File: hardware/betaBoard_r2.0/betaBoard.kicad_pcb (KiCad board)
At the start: 2 copper layers, 70 x 45 mm, 141 parts, among them J1 DNP, J2 AMPHENOL_10103592-0001LF, J3 DNP, J4 DNP, J5 DNP, J6 DNP, SW1 TS-1187A-B-A-B, SW2 TS-1187A-B-A-B, U1 AMS1117-3.3_SOT223, U2 W25Q128JVSIQ, U3 RP2040, U4 LM358, U5 LM358, U6 LM358, U7 LM358, Y1 X322512MSB4SI

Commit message: main r2.0 design done
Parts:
- removed C35, C41: 47p, Capacitor_SMD:C_0603_1608Metric
- removed C36: 100n, Capacitor_SMD:C_0603_1608Metric
- removed C37, C38: 10p, Capacitor_SMD:C_0603_1608Metric
- removed C39: 470n, Capacitor_SMD:C_0603_1608Metric
- removed C40: 1u, Capacitor_SMD:C_0603_1608Metric
- removed C42: 10u, Capacitor_SMD:C_1206_3216Metric
- removed C44, C46, C47: 10u, Capacitor_SMD:C_0603_1608Metric
- removed D16: DNP, OptoDevice:Osram_BPW34S-SMD
- removed D17, D18, D24, D25: 1N5819WS, Diode_SMD:D_SOD-323
- removed D20, D22, D23: ZMM3V3-M, Diode_SMD:D_MiniMELF
- removed J1: DNP, betaBoard:PinHeader_1x02_P2.54mm_castellation
- removed J3: DNP, Connector_PinSocket_2.54mm:PinSocket_1x02_P2.54mm_Vertical
- removed JP1: DNP, Jumper:SolderJumper-2_P1.3mm_Bridged2Bar_Pad1.0x1.5mm
- removed U7: LM358, Package_SO:SOIC-8_3.9x4.9mm_P1.27mm
- added H7: M3 Hole, MountingHole:MountingHole_2.7mm_M2.5_DIN965_Pad, F.Cu at (90.0, 53.0)
- added H8: M3 Hole, MountingHole:MountingHole_2.7mm_M2.5_DIN965_Pad, F.Cu at (53.0, 97.0)
- added H9: M3 Hole, MountingHole:MountingHole_2.7mm_M2.5_DIN965_Pad, F.Cu at (53.0, 53.0)
- C1: value 10u -> 100u
- C19, C31: value 10p -> 100n
- C20, C32: value 10p -> 1u
- C21, C33: value 470n -> 10p
- C22: value 1u -> 100u; footprint Capacitor_SMD:C_0603_1608Metric -> Capacitor_SMD:C_1206_3216Metric
- C23: value 47p -> 100n
- C25: value 10p -> 10u
- C26: value 10p -> 2p2
- C27: value 470n -> 100n
- C29: value 47p -> 10p
- C30: value 100n -> 10p
- C34: value 1u -> 10p
- D1, D13, D5, D9: moved to F.Cu
- D10, D11, D14, D6, D7: value BPW34-SMD -> ZMM3V3-M; footprint betaBoard:Osram_BPW34S-SMD_hole -> Diode_SMD:D_MiniMELF
- D12, D4, D8: value DNP -> ZMM3V3-M; footprint OptoDevice:Osram_BPW34S-SMD -> Diode_SMD:D_MiniMELF; moved to F.Cu
- D15, D2, D3: value BPW34-SMD -> DNP; footprint betaBoard:Osram_BPW34S-SMD_hole -> OptoDevice:Osram_BPW34S-SMD
- R13, R21: value 47k -> 1k
- R14, R22, R30: value 150k -> 10k
- R15, R31: value 47M -> 10k
- R16, R24: value 4K7 -> 1k
- R17: value 10k -> 1k
- R19, R27: value 1M -> 100k
- R2, R3, R4, R5: value 1k -> 10k
- R23: value 47M -> 22M
- R26, R41, R42, R44: value 10k -> 100k
- R29: value 47k -> 10k
- R32, R40: value 4K7 -> 10k
- R33: value 10k -> 4R7
- R34, R36: value 10k -> 0
- R35: value 1M -> 1k
- R37: value 47k -> 10M
- R38: value 150k -> 1k
- R39: value 47M -> 1k
- R43: value 1M -> 10k
- R45: value 0 -> DNP
- U4, U5, U6: value LM358 -> MCP6232
- moved H6 75.7 mm to (116.0, 92.5)
- moved H5 70.7 mm to (57.5, 97.0)
- moved R31 40.2 mm to (61.8, 75.5), turned to -90 degrees
- moved H4 37.3 mm to (56.5, 56.0)
- moved R32 33.1 mm to (63.4, 75.5)
- moved C34 32.5 mm to (110.9, 89.0), turned to 180 degrees
- moved R30 31.8 mm to (76.2, 81.8), turned to -90 degrees
- moved R29 31.8 mm to (77.7, 81.8)
- moved R36 29.8 mm to (110.9, 85.8), turned to 0 degrees
- moved D12 28.1 mm to (95.3, 88.7)
- moved C25 27.2 mm to (110.9, 84.2), turned to 0 degrees
- moved R44 26.6 mm to (110.9, 90.7), turned to 0 degrees
- moved D14 26.3 mm to (93.0, 88.7), turned to 90 degrees
- moved C22 25.8 mm to (96.1, 58.7), turned to 180 degrees
- moved D5 25.7 mm to (116.8, 61.3), turned to 90 degrees
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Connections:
- C1 pad 1: /LDO_IN -> /5V_USB
- C19 pad 1: /particle_sensor_array/Diodes -> Net-(U4B-+)
- C20 pad 1: Net-(C19-Pad2) -> Net-(U4A-+)
- C20 pad 2: Net-(C20-Pad2) -> GND
- C21 pad 1: Net-(C20-Pad2) -> Net-(U4A--)
- C22 pad 1: Net-(U4B-+) -> VCC
- C23 pad 1: Net-(U4B--) -> VCC
- C23 pad 2: Net-(C23-Pad2) -> GND
- C25 pad 1: /particle_sensor_array1/Diodes -> Net-(D11-K)
- C25 pad 2: Net-(C25-Pad2) -> GND
- C26 pad 1: Net-(C25-Pad2) -> Net-(U5A--)
- C26 pad 2: Net-(C26-Pad2) -> Net-(U4B-+)
- C27 pad 1: Net-(C26-Pad2) -> Net-(U4B-+)
- C30 pad 1: VCC -> Net-(U6A--)
- C30 pad 2: GND -> Net-(C30-Pad2)
- C31 pad 1: /particle_sensor_array2/Diodes -> Net-(C31-Pad1)
- C32 pad 1: Net-(C31-Pad2) -> Net-(U6B-+)
- C32 pad 2: Net-(C32-Pad2) -> GND
- C33 pad 1: Net-(C32-Pad2) -> Net-(U6B--)
- C34 pad 1: Net-(U6B-+) -> Net-(C30-Pad2)
- C34 pad 2: GND -> Net-(C31-Pad1)
- C45 pad 1: Net-(U5A-+) -> Net-(D4-K)
- D10 pad 1: /particle_sensor_array2/Diodes -> /MCU/ADC1
- D11 pad 1: /particle_sensor_array3/Diodes -> Net-(D11-K)
- D14 pad 1: /particle_sensor_array2/Diodes -> /Frontend Alpha/out
- D15 pad 1: /particle_sensor_array3/Diodes -> /Frontend Alpha/Diodes
- D2 pad 1: /particle_sensor_array2/Diodes -> /particle_sensor_array1/Diodes
- D3 pad 1: /particle_sensor_array3/Diodes -> /particle_sensor_array1/Diodes
- D4 pad 1: Net-(D12-K) -> Net-(D4-K)
- D6 pad 1: /particle_sensor_array2/Diodes -> Net-(D6-K)
- D7 pad 1: /particle_sensor_array3/Diodes -> /MCU/ADC2
- D8 pad 1: Net-(D12-K) -> Net-(D8-K)
- J4 pad 2: /MCU/UART0_RX -> Net-(J4-Pin_2)
- J4 pad 3: /MCU/UART0_TX -> Net-(J4-Pin_3)
- J5 pad 1: /MCU/SWD_CLK -> Net-(J5-Pin_1)
- J5 pad 3: /MCU/SWD_SIO -> Net-(J5-Pin_3)
- R13 pad 2: Net-(U4A-+) -> Net-(D6-K)
- R14 pad 1: Net-(U4A-+) -> /MCU/ADC2
- R14 pad 2: GND -> Net-(U4B--)
- R15 pad 1: Net-(C20-Pad2) -> /MCU/ADC2
- R15 pad 2: /particle_sensor_array/Diodes -> GND
- R16 pad 1: Net-(U4B--) -> VCC
- R16 pad 2: Net-(C21-Pad2) -> Net-(D8-K)
- R17 pad 1: Net-(U4B-+) -> Net-(U4A--)
- R17 pad 2: +3V3 -> Net-(C19-Pad2)
- R18 pad 1: GND -> Net-(U4A-+)
- R18 pad 2: Net-(U4B-+) -> Net-(D8-K)
- R19 pad 1: Net-(C23-Pad2) -> GND
- R19 pad 2: Net-(U4B--) -> Net-(U4A-+)
- R2 pad 1: /MCU/GP10 -> /MCU/GP13
- R20 pad 1: /MCU/ADC0 -> Net-(C21-Pad2)
- R20 pad 2: Net-(C23-Pad2) -> Net-(U4A--)
- R21 pad 2: Net-(U5A-+) -> Net-(D4-K)
- R22 pad 1: Net-(U5A-+) -> /MCU/ADC1
- R22 pad 2: GND -> Net-(C21-Pad2)
- R23 pad 1: Net-(C26-Pad2) -> Net-(U4B-+)
- R23 pad 2: /particle_sensor_array1/Diodes -> Net-(U5A--)
- R25 pad 2: +3V3 -> Net-(D6-K)
- R29 pad 1: VCC -> /MCU/SWD_SIO
- R29 pad 2: Net-(U6A-+) -> Net-(J5-Pin_3)
- R3 pad 1: /MCU/GP11 -> /MCU/GP12
- R30 pad 1: Net-(U6A-+) -> /MCU/SWD_CLK
- R30 pad 2: GND -> Net-(J5-Pin_1)
- R31 pad 1: Net-(C32-Pad2) -> /MCU/UART0_TX
- R31 pad 2: /particle_sensor_array2/Diodes -> Net-(J4-Pin_3)
- R32 pad 1: Net-(U6B--) -> /MCU/UART0_RX
- R32 pad 2: Net-(C33-Pad2) -> Net-(J4-Pin_2)
- R33 pad 1: Net-(U6B-+) -> VCC
- R33 pad 2: +3V3 -> /5V_USB
- R34 pad 1: GND -> Net-(U5A--)
- R34 pad 2: Net-(U6B-+) -> /particle_sensor_array1/Diodes
- R35 pad 1: Net-(C35-Pad2) -> VCC
- R35 pad 2: Net-(U6B--) -> Net-(D11-K)
- R36 pad 1: /MCU/ADC2 -> Net-(U6A--)
- R36 pad 2: Net-(C35-Pad2) -> /Frontend Alpha/Diodes
- R37 pad 1: VCC -> Net-(C31-Pad1)
- R37 pad 2: Net-(U7A-+) -> Net-(U6A--)
- R38 pad 1: Net-(U7A-+) -> VCC
- R38 pad 2: GND -> Net-(D12-K)
- R39 pad 1: Net-(C38-Pad2) -> Net-(U6B--)
- R39 pad 2: /particle_sensor_array3/Diodes -> Net-(C31-Pad2)
- R4 pad 1: /MCU/GP12 -> /MCU/GP11
- R40 pad 1: Net-(U7B--) -> Net-(U6B-+)
- R40 pad 2: Net-(C39-Pad2) -> Net-(D12-K)
- R41 pad 1: Net-(U7B-+) -> GND
- R41 pad 2: +3V3 -> Net-(U6B-+)
- R42 pad 1: GND -> Net-(C33-Pad2)
- R42 pad 2: Net-(U7B-+) -> Net-(U6B--)
- R43 pad 1: Net-(C41-Pad2) -> /Frontend Alpha/out
- R43 pad 2: Net-(U7B--) -> Net-(C33-Pad2)
- R44 pad 1: /MCU/ADC1 -> /Frontend Alpha/out_bias
- R44 pad 2: Net-(C41-Pad2) -> Net-(C31-Pad1)
- R5 pad 1: /MCU/GP13 -> /MCU/GP10
- U1 pad 3: /LDO_IN -> /5V_USB
- U3 pad 35: unconnected-(U3-GPIO23-Pad35) -> /Frontend Alpha/out_bias
- U3 pad 38: /MCU/ADC0 -> /Frontend Alpha/out
- U4 pad 1: Net-(C20-Pad2) -> Net-(C21-Pad2)
- U4 pad 2: /particle_sensor_array/Diodes -> Net-(U4A--)
- U4 pad 7: Net-(C23-Pad2) -> Net-(U4B--)
- U5 pad 1: Net-(C26-Pad2) -> Net-(U4B-+)
- U5 pad 2: /particle_sensor_array1/Diodes -> Net-(U5A--)
- U5 pad 3: Net-(U5A-+) -> Net-(D4-K)
- U6 pad 1: Net-(C32-Pad2) -> Net-(C31-Pad1)
- U6 pad 2: /particle_sensor_array2/Diodes -> Net-(U6A--)
- U6 pad 3: Net-(U6A-+) -> Net-(D11-K)
- U6 pad 7: Net-(C35-Pad2) -> Net-(C33-Pad2)
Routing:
- net /Frontend Alpha/out_bias: track 0.00 -> 50.8 mm
- net +3V3: track 221.9 -> 172.4 mm, vias 9 -> 4
- net /Frontend Alpha/out: track 0.00 -> 38.5 mm
- net Net-(D12-K): track 37.1 -> 4.67 mm, vias 1 -> 0
- net VCC: track 120.5 -> 92.6 mm
- net /MCU/ADC0: track 26.5 -> 0.00 mm
- net /5V_USB: track 16.9 -> 39.8 mm, vias 0 -> 4
- net /particle_sensor_array3/Diodes: track 22.5 -> 0.00 mm
- net /particle_sensor_array2/Diodes: track 21.9 -> 0.00 mm
- net /particle_sensor_array/Diodes: track 20.2 -> 0.00 mm
- net /particle_sensor_array1/Diodes: track 38.8 -> 19.2 mm, vias 1 -> 0
- net /MCU/ADC1: track 17.6 -> 33.9 mm, vias 0 -> 2
- net Net-(U4A--): track 0.00 -> 16.2 mm
- net Net-(C31-Pad1): track 0.00 -> 14.3 mm
- net /Frontend Alpha/Diodes: track 0.00 -> 13.2 mm
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- added copper zone on B.Cu, net /5V_USB
- added copper zone on F.Cu, net /5V_USB
- removed copper zone on F.Cu, net /LDO_IN
- removed copper zone on B.Cu, net VCC
- removed copper zone on F.Cu, net VCC
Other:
- board size 70 x 45 mm -> 80 x 50 mm
- board text added: "Accepted DRC Error: - USB port: 3 errors - Boot Select button: 1 error"
- board text added: "Alpha"
- board text added: "betaBoard R2.0 Demonostration Particle Detector 2024 Kuhlbusch"
- board text removed: "+"
- board text removed: "-"
- board text removed: "5-12V"
- board text removed: "Castellations produce 2 errors in DRC"
- board text removed: "Details: https://github.com/timbk/BetaBoard"
- board text removed: "Unmarked 0603 are mostly 100nF"
- board text removed: "betaBoard R1.1 Demonostration Particle Detector 2023 Kuhlbusch"

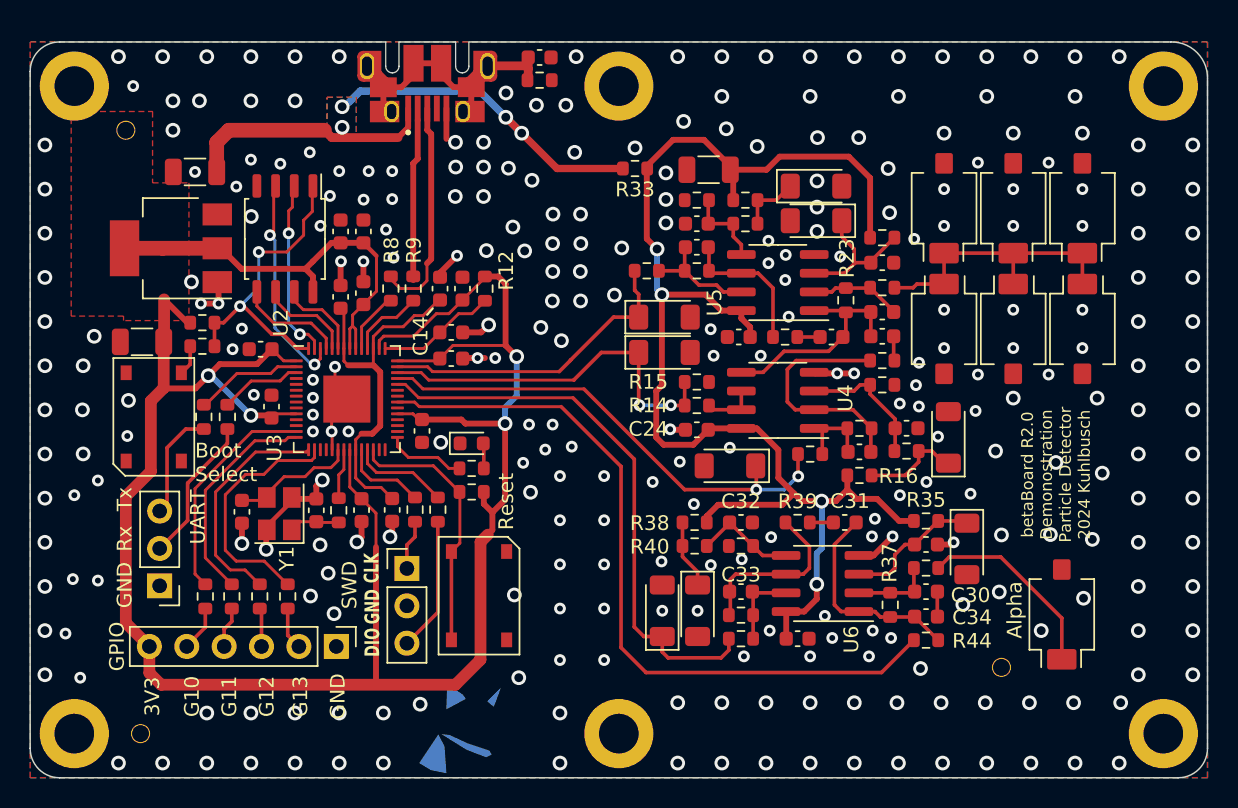
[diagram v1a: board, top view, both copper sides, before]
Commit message: hardware: updated kicad version
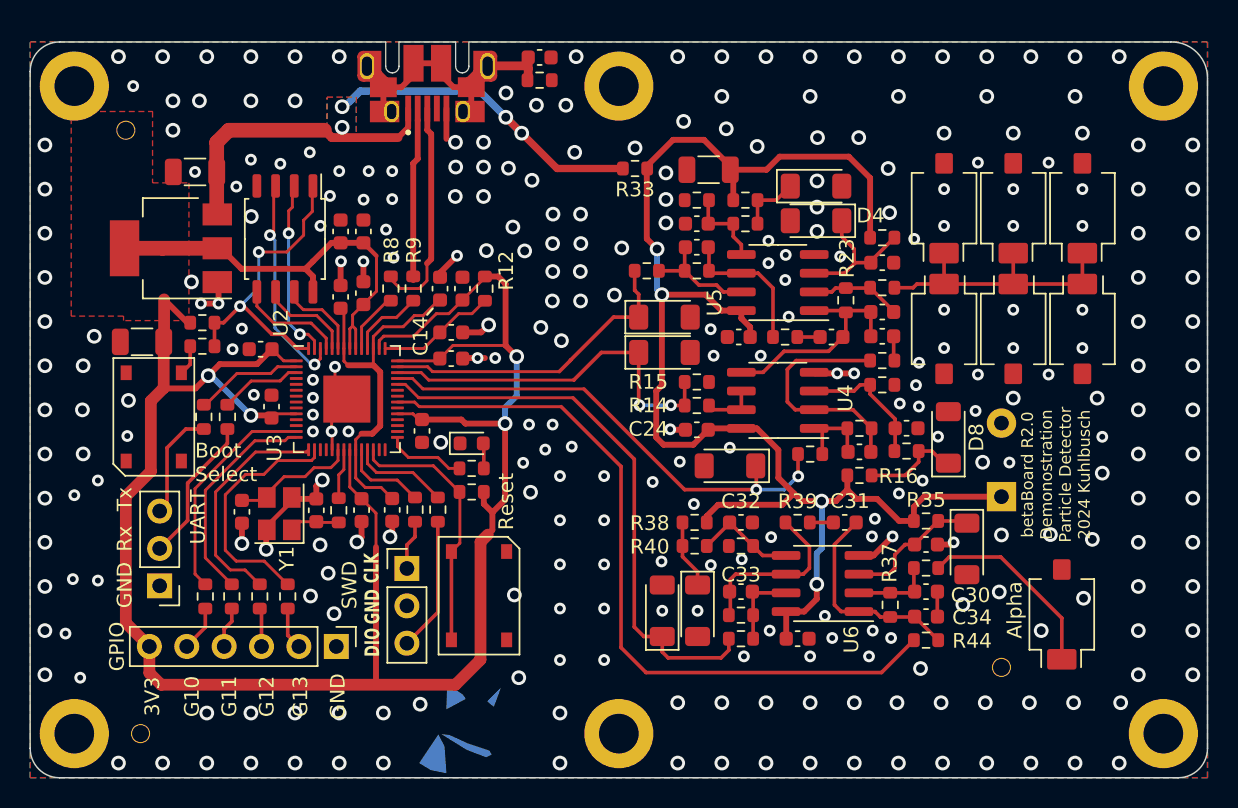
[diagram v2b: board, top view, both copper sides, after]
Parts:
- added C35: DNP, Capacitor_THT:CP_Radial_D10.0mm_P5.00mm, B.Cu at (116.0, 80.9)
- C20, C28: value 1u -> 10u
- D1, D13, D15, D2, D3, D5, D9: value DNP -> BPW34
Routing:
- net VCC: track 92.6 -> 99.8 mm
- net /5V_USB: track 39.8 -> 42.7 mm
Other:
- board text added: "D8"
- board text added: "Sensor requires absolute darkness!"
- board text removed: "Requires absolute darkness!"
